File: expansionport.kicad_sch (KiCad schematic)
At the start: 18 parts, among them J20 C64_Expansion_Port, U31 74LS04, U32 74LVC374, U33 74LVC374, U34 74LVC374, U35 74LS374, U36 74LS374, U37 74LS374, U38 74LVC374, U39 74LVC374, U40 74LS374, U41 74LS374, U42 74LS06

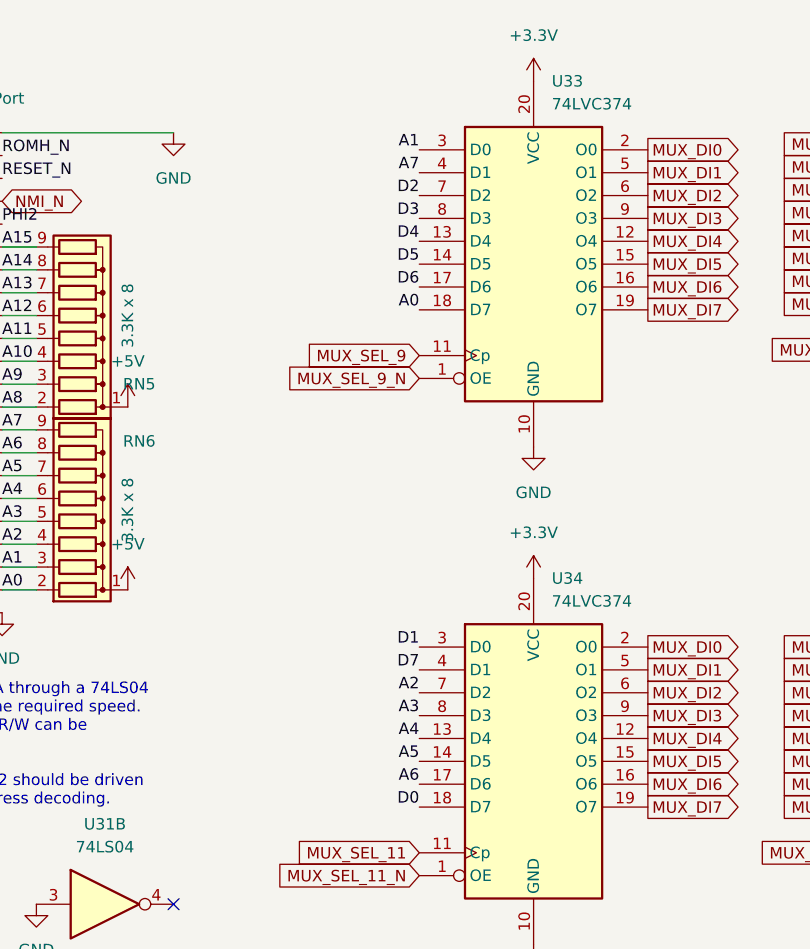
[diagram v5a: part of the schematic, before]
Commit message: more cart and mux bus layout
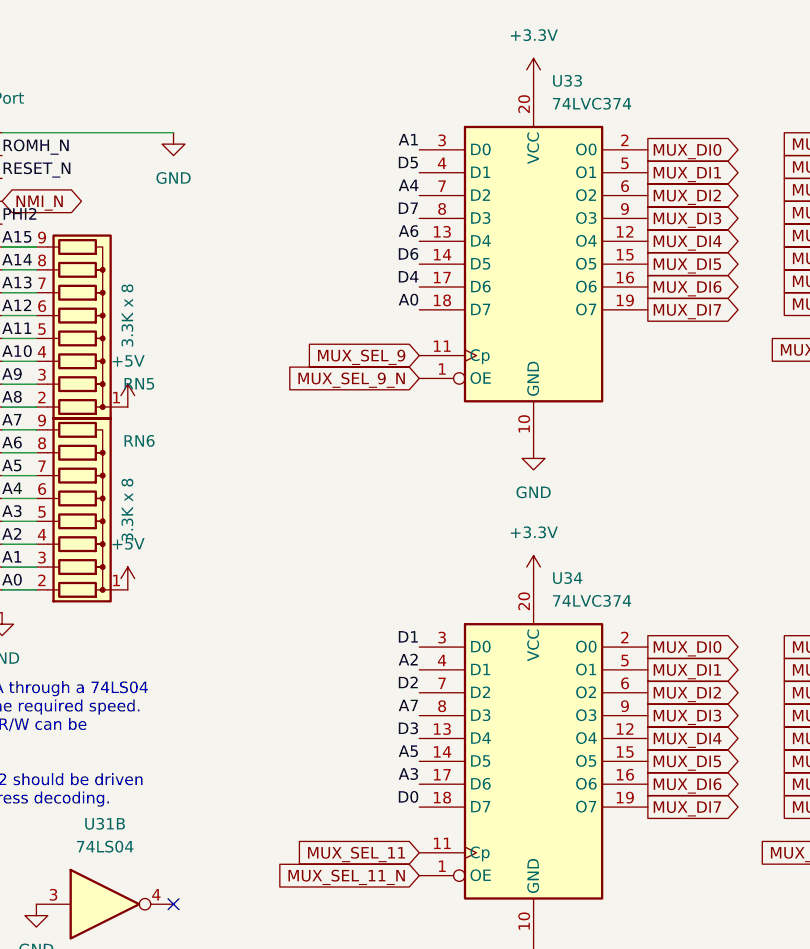
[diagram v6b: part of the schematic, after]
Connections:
- net A2: now also U34.4 (D1); no longer U34.7 (D2)
- net A3: now also U34.17 (D6); no longer U34.8 (D3)
- net A4: now also U33.7 (D2); no longer U34.13 (D4)
- net A6: now also U33.13 (D4); no longer U34.17 (D6)
- net A7: now also U34.8 (D3); no longer U33.4 (D1)
- net D2: now also U34.7 (D2); no longer U33.7 (D2)
- net D3: now also U34.13 (D4); no longer U33.8 (D3)
- net D4: now also U33.17 (D6); no longer U33.13 (D4)
- net D5: now also U33.4 (D1); no longer U33.14 (D5)
- net D6: now also U33.14 (D5); no longer U33.17 (D6)
- net D7: now also U33.8 (D3); no longer U34.4 (D1)
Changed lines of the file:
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@@
     (effects (font (size 1.27 1.27)) (justify right bottom))
   )
-  (label "D2" (at 103.505 33.655 180)
+  (label "D2" (at 103.505 88.9 180)
     (effects (font (size 1.27 1.27)) (justify right bottom))
   )
@@
     (effects (font (size 1.27 1.27)) (justify right bottom))
   )
-  (label "A4" (at 103.505 93.98 180)
+  (label "A4" (at 103.505 33.655 180)
     (effects (font (size 1.27 1.27)) (justify right bottom))
   )
@@
     (effects (font (size 1.27 1.27)) (justify left bottom))
   )
-  (label "A3" (at 103.505 91.44 180)
+  (label "A3" (at 103.505 99.06 180)
     (effects (font (size 1.27 1.27)) (justify right bottom))
   )
@@
     (effects (font (size 1.27 1.27)) (justify right bottom))
   )
-  (label "D7" (at 103.505 86.36 180)
+  (label "D7" (at 103.505 36.195 180)
     (effects (font (size 1.27 1.27)) (justify right bottom))
   )
@@
     (effects (font (size 1.27 1.27)) (justify left bottom))
   )
-  (label "A2" (at 103.505 88.9 180)
+  (label "A2" (at 103.505 86.36 180)
     (effects (font (size 1.27 1.27)) (justify right bottom))
   )
@@
     (effects (font (size 1.27 1.27)) (justify left bottom))
   )
-  (label "A6" (at 103.505 99.06 180)
+  (label "A6" (at 103.505 38.735 180)
     (effects (font (size 1.27 1.27)) (justify right bottom))
   )
@@
     (effects (font (size 1.27 1.27)) (justify left bottom))
   )
-  (label "D3" (at 103.505 36.195 180)
+  (label "D3" (at 103.505 93.98 180)
     (effects (font (size 1.27 1.27)) (justify right bottom))
   )
@@
     (effects (font (size 1.27 1.27)) (justify left bottom))
   )
-  (label "A7" (at 103.505 31.115 180)
+  (label "A7" (at 103.505 91.44 180)
     (effects (font (size 1.27 1.27)) (justify right bottom))
   )
@@
     (effects (font (size 1.27 1.27)) (justify left bottom))
   )
-  (label "D4" (at 103.505 38.735 180)
+  (label "D4" (at 103.505 43.815 180)
     (effects (font (size 1.27 1.27)) (justify right bottom))
   )
@@
     (effects (font (size 1.27 1.27)) (justify left bottom))
   )
-  (label "D6" (at 103.505 43.815 180)
-    (effects (font (size 1.27 1.27)) (justify right bottom))
-  )
-  (label "D5" (at 103.505 41.275 180)
-    (effects (font (size 1.27 1.27)) (justify right bottom))
-  )
+  (label "D6" (at 103.505 41.275 180)
+    (effects (font (size 1.27 1.27)) (justify right bottom))
+  )
+  (label "D5" (at 103.505 31.115 180)
+    (effects (font (size 1.27 1.27)) (justify right bottom))
+  )

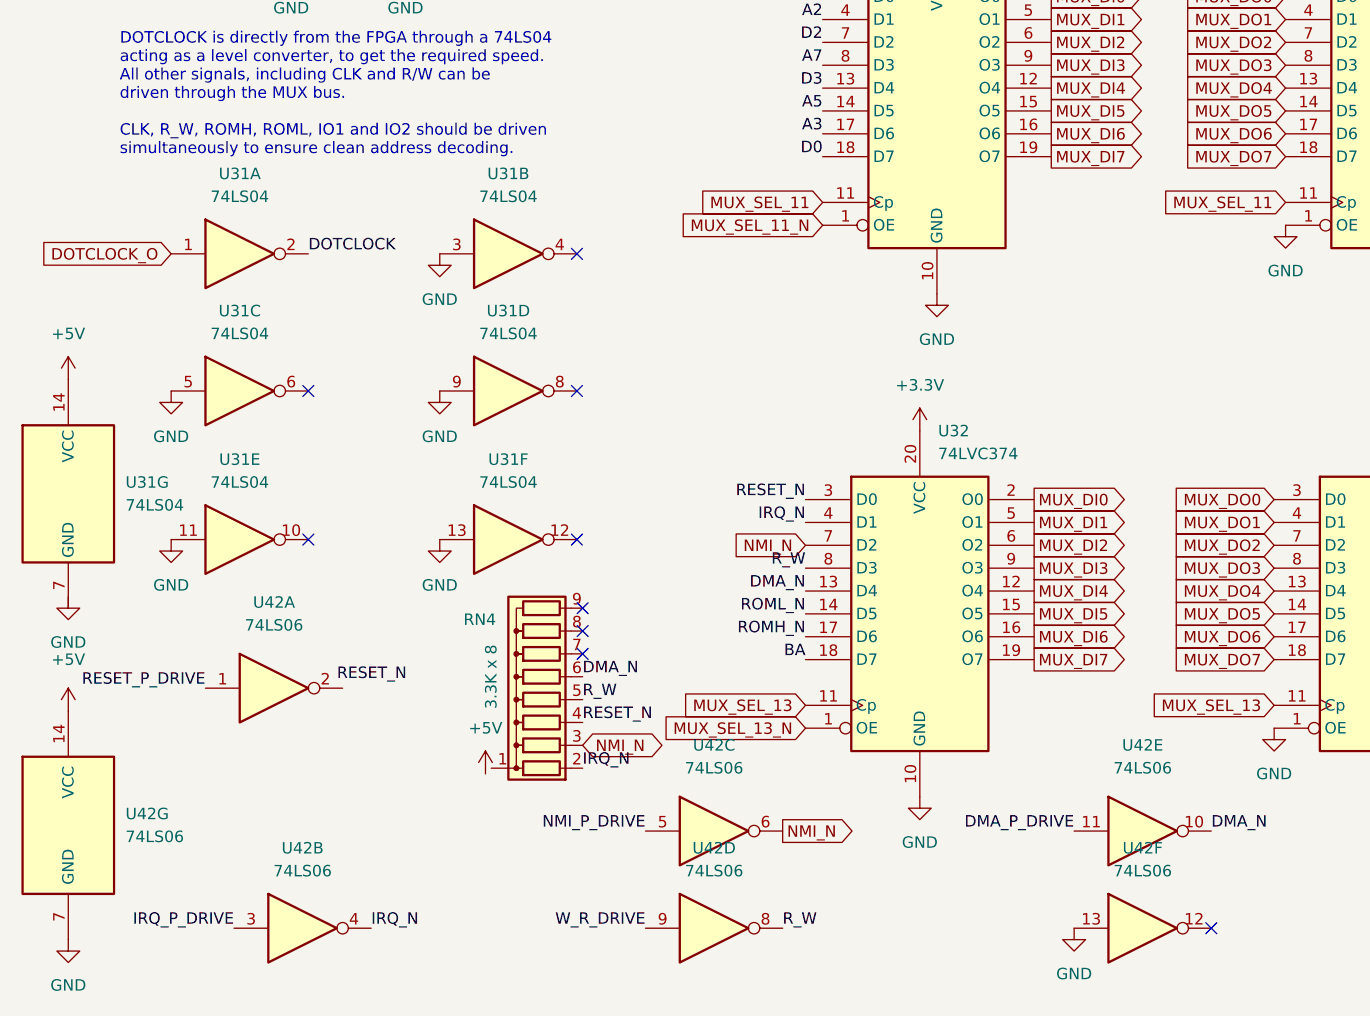
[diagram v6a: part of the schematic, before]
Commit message: route IEC port. Remove duplicate footprints
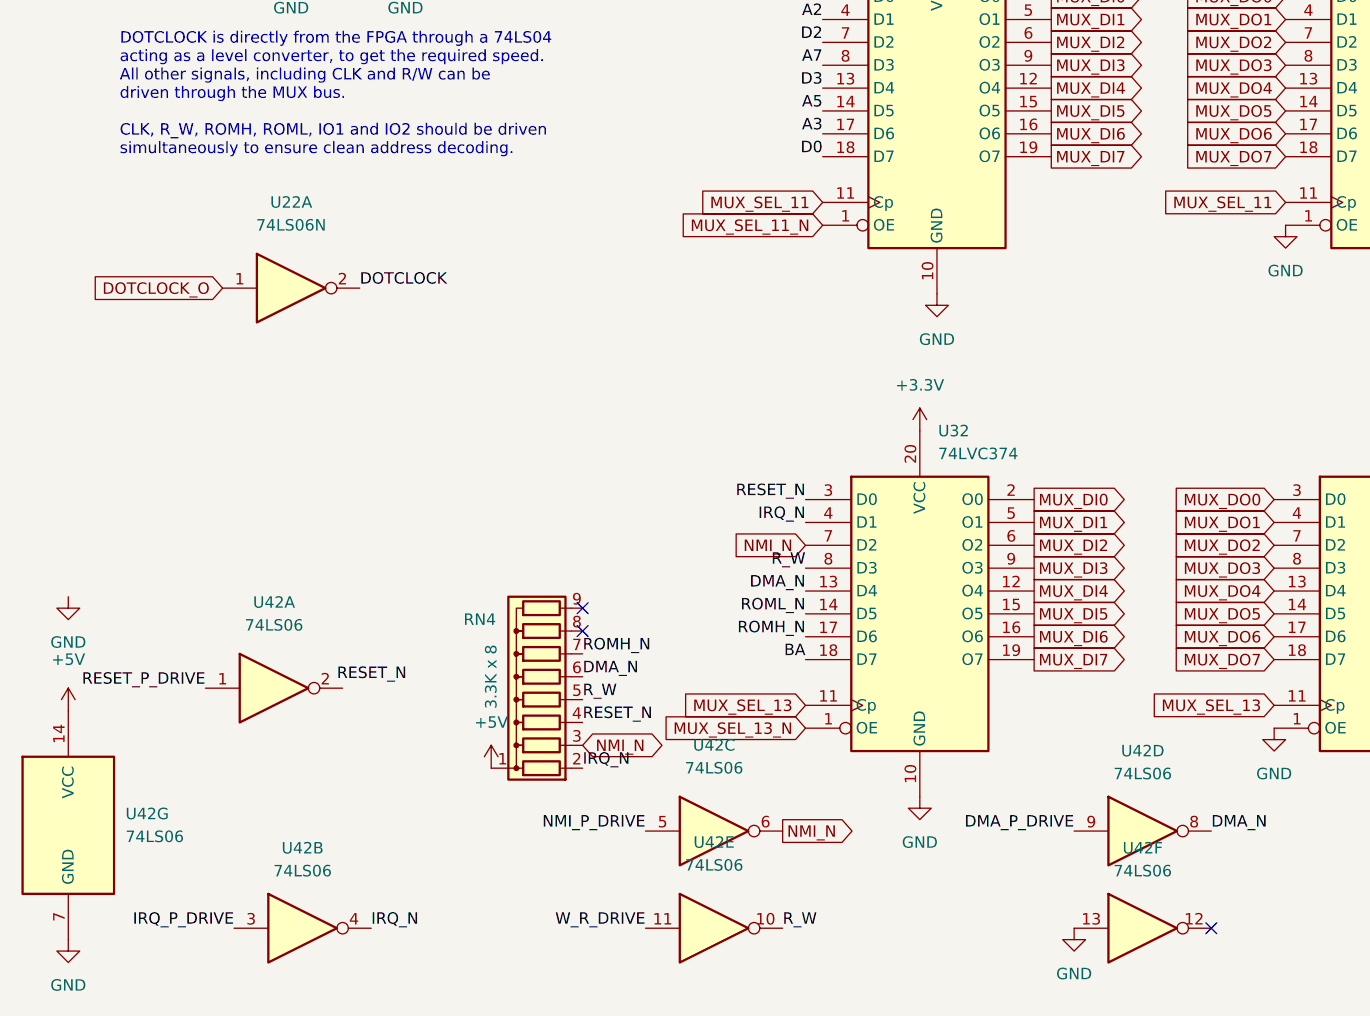
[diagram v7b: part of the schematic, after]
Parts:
- removed U31: 74LS04, Package_DIP:DIP-14_W7.62mm, symbol 74xx:74LS04
- added U22: 74LS06N, Package_DIP:DIP-14_W7.62mm, symbol 74xx:74LS06N
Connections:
- net +5V: now also RN4.1 (common)
- net DMA_N: now also U42.8; no longer U42.10
- net DMA_P_DRIVE: now also U42.9; no longer U42.11
- net DOTCLOCK: now also U22.2
- net DOTCLOCK_O: now also U22.1
- net ROMH_N: now also RN4.7 (R6)
- net R_W: now also U42.10; no longer U42.8
- net W_R_DRIVE: now also U42.11; no longer U42.9
- no-connect marks 23 -> 17
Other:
- moved on the sheet: U42D, U42E

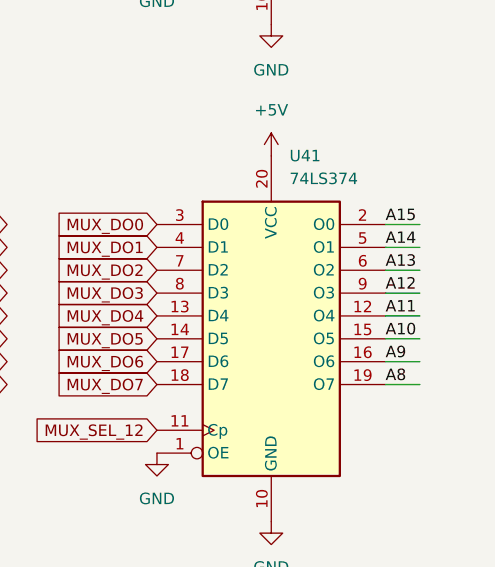
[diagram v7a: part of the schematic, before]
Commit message: route more cart port
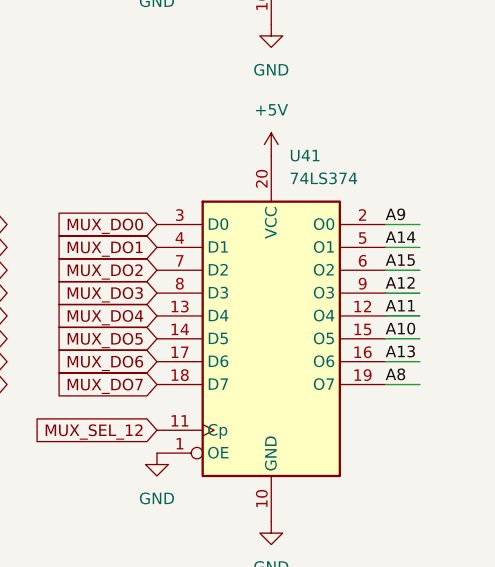
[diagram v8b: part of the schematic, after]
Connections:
- net A13: now also U41.16 (O6); no longer U41.6 (O2)
- net A15: now also U41.6 (O2); no longer U41.2 (O0)
- net A9: now also U41.2 (O0); no longer U41.16 (O6)
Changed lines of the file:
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@@
     (effects (font (size 1.27 1.27)) (justify left bottom))
   )
-  (label "A15" (at 275.59 83.82 0)
+  (label "A15" (at 275.59 88.9 0)
     (effects (font (size 1.27 1.27)) (justify left bottom))
   )
@@
     (effects (font (size 1.27 1.27)) (justify right bottom))
   )
-  (label "A13" (at 275.59 88.9 0)
+  (label "A13" (at 275.59 99.06 0)
     (effects (font (size 1.27 1.27)) (justify left bottom))
   )
@@
     (effects (font (size 1.27 1.27)) (justify right bottom))
   )
-  (label "A9" (at 275.59 99.06 0)
+  (label "A9" (at 275.59 83.82 0)
     (effects (font (size 1.27 1.27)) (justify left bottom))
   )
